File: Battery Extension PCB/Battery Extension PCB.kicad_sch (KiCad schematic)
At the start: 30 parts, among them P1 Solder_Pad, P2 Solder_Pad, U1 M1250RS-02P, U2 S8050, U3 FS8205A, U4 TPS61032PWPR, U5 TP4056, U6 DW01A, U7 FXL0530-6R8-M

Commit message: updated pcb files
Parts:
- H1, H2, H3, H4, H5, H6, H7: footprint footprint:Castellated hole large -> footprint:Castellated hole
- U4: footprint footprint:HTSSOP-16_L5.0-W4.4-P0.65-LS6.4-BL-EP -> Package_SO:HTSSOP-16-1EP_4.4x5mm_P0.65mm_EP3.4x5mm_Mask2.46x2.31mm
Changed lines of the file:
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@@
       (effects (font (size 1.27 1.27)) (justify left))
     )
-    (property "Footprint" "footprint:Castellated hole large" (id 2) (at 207.01 69.85 0)
+    (property "Footprint" "footprint:Castellated hole" (id 2) (at 207.01 69.85 0)
       (effects (font (size 1.27 1.27)) hide)
     )
@@
       (effects (font (size 1.27 1.27)) (justify left))
     )
-    (property "Footprint" "footprint:Castellated hole large" (id 2) (at 207.01 88.9 0)
+    (property "Footprint" "footprint:Castellated hole" (id 2) (at 207.01 88.9 0)
       (effects (font (size 1.27 1.27)) hide)
     )
@@
       (effects (font (size 1.27 1.27)) (justify left))
     )
-    (property "Footprint" "footprint:Castellated hole large" (id 2) (at 207.01 95.25 0)
+    (property "Footprint" "footprint:Castellated hole" (id 2) (at 207.01 95.25 0)
       (effects (font (size 1.27 1.27)) hide)
     )
@@
       (effects (font (size 1.27 1.27)) (justify left))
     )
-    (property "Footprint" "footprint:Castellated hole large" (id 2) (at 207.01 57.15 0)
+    (property "Footprint" "footprint:Castellated hole" (id 2) (at 207.01 57.15 0)
       (effects (font (size 1.27 1.27)) hide)
     )
@@
       (effects (font (size 1.27 1.27)) (justify left))
     )
-    (property "Footprint" "footprint:Castellated hole large" (id 2) (at 207.01 82.55 0)
+    (property "Footprint" "footprint:Castellated hole" (id 2) (at 207.01 82.55 0)
       (effects (font (size 1.27 1.27)) hide)
     )
@@
     (property "Reference" "U4" (id 0) (at 92.71 132.08 0))
     (property "Value" "TPS61032PWPR" (id 1) (at 92.71 134.62 0))
-    (property "Footprint" "footprint:HTSSOP-16_L5.0-W4.4-P0.65-LS6.4-BL-EP" (id 2) (at 92.71 133.35 0)
+    (property "Footprint" "Package_SO:HTSSOP-16-1EP_4.4x5mm_P0.65mm_EP3.4x5mm_Mask2.46x2.31mm" (id 2) (at 92.71 133.35 0)
       (effects (font (size 1.27 1.27) italic) hide)
     )
@@
       (effects (font (size 1.27 1.27)) (justify left))
     )
-    (property "Footprint" "footprint:Castellated hole large" (id 2) (at 207.01 76.2 0)
+    (property "Footprint" "footprint:Castellated hole" (id 2) (at 207.01 76.2 0)
       (effects (font (size 1.27 1.27)) hide)
     )
@@
       (effects (font (size 1.27 1.27)) (justify left))
     )
-    (property "Footprint" "footprint:Castellated hole large" (id 2) (at 207.01 63.5 0)
+    (property "Footprint" "footprint:Castellated hole" (id 2) (at 207.01 63.5 0)
       (effects (font (size 1.27 1.27)) hide)
     )
@@
     )
     (path "/772c5c6f-179b-4fe8-8e39-b42331ec6892"
-      (reference "H1") (unit 1) (value "Castellated_hole") (footprint "footprint:Castellated hole large")
+      (reference "H1") (unit 1) (value "Castellated_hole") (footprint "footprint:Castellated hole")
     )
     (path "/d9dac4f3-7e11-4f08-aac0-c6a976f30cbb"
-      (reference "H2") (unit 1) (value "Castellated_hole") (footprint "footprint:Castellated hole large")
+      (reference "H2") (unit 1) (value "Castellated_hole") (footprint "footprint:Castellated hole")
     )
     (path "/0db3ddba-901d-4b77-a11a-030a5807c4d2"
-      (reference "H3") (unit 1) (value "Castellated_hole") (footprint "footprint:Castellated hole large")
+      (reference "H3") (unit 1) (value "Castellated_hole") (footprint "footprint:Castellated hole")
     )
     (path "/bfa42e2b-26ca-441e-87fc-b5c3c76d771e"
-      (reference "H4") (unit 1) (value "Castellated_hole") (footprint "footprint:Castellated hole large")
+      (reference "H4") (unit 1) (value "Castellated_hole") (footprint "footprint:Castellated hole")
     )
     (path "/a78caffe-a774-45f9-b997-1377730563d7"
-      (reference "H5") (unit 1) (value "Castellated_hole") (footprint "footprint:Castellated hole large")
+      (reference "H5") (unit 1) (value "Castellated_hole") (footprint "footprint:Castellated hole")
     )
     (path "/1972109c-d6a8-439a-8ba3-88c8e6bb7196"
-      (reference "H6") (unit 1) (value "Castellated_hole") (footprint "footprint:Castellated hole large")
+      (reference "H6") (unit 1) (value "Castellated_hole") (footprint "footprint:Castellated hole")
     )
     (path "/37c5e4f3-7cb5-4ef4-9c9d-447ed0599cb8"
-      (reference "H7") (unit 1) (value "Castellated_hole") (footprint "footprint:Castellated hole large")
+      (reference "H7") (unit 1) (value "Castellated_hole") (footprint "footprint:Castellated hole")
     )
     (path "/ae26b445-daff-423c-875c-0c8c4d475a5f"
@@
     )
     (path "/b3294315-f1f5-4699-9d26-423f0a5d1bc5"
-      (reference "U4") (unit 1) (value "TPS61032PWPR") (footprint "footprint:HTSSOP-16_L5.0-W4.4-P0.65-LS6.4-BL-EP")
+      (reference "U4") (unit 1) (value "TPS61032PWPR") (footprint "Package_SO:HTSSOP-16-1EP_4.4x5mm_P0.65mm_EP3.4x5mm_Mask2.46x2.31mm")
     )
     (path "/94c4b137-5d1b-45eb-9fd3-3bc14acb67a1"

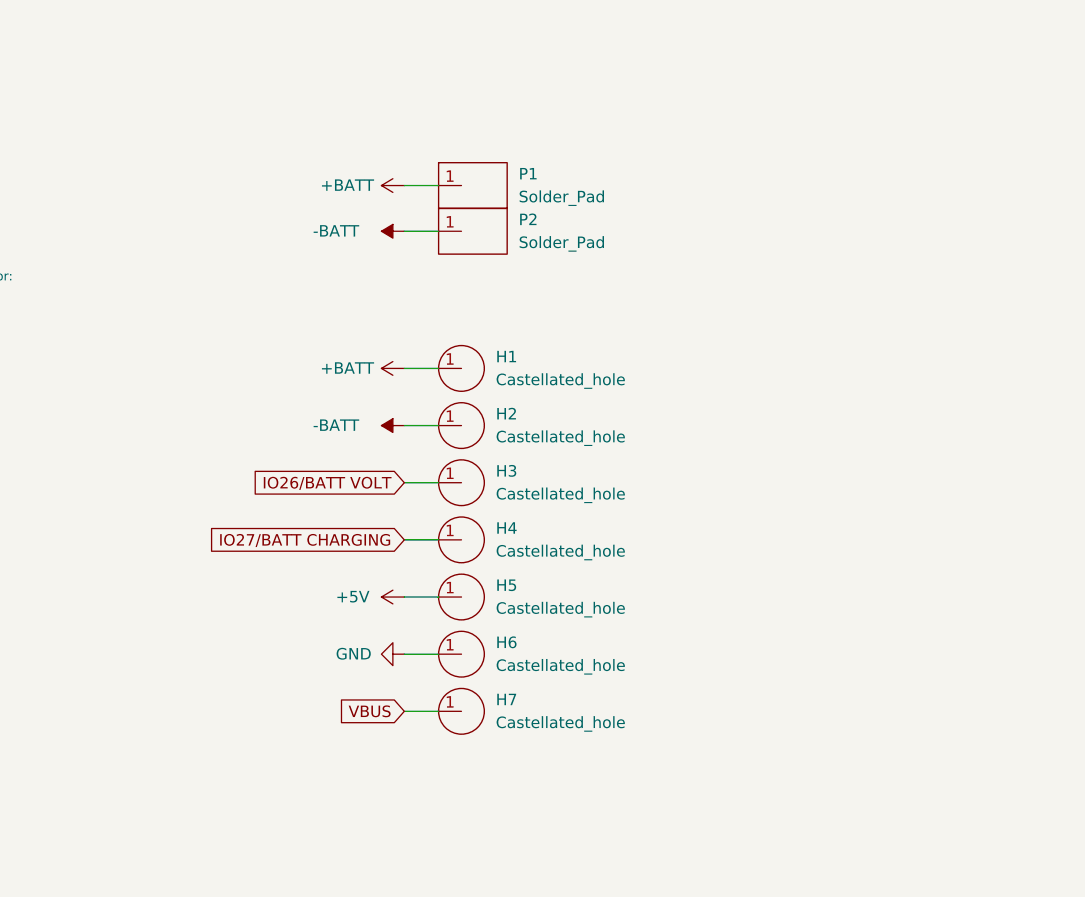
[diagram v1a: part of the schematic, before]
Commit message: replaced castallated holes with solder pads
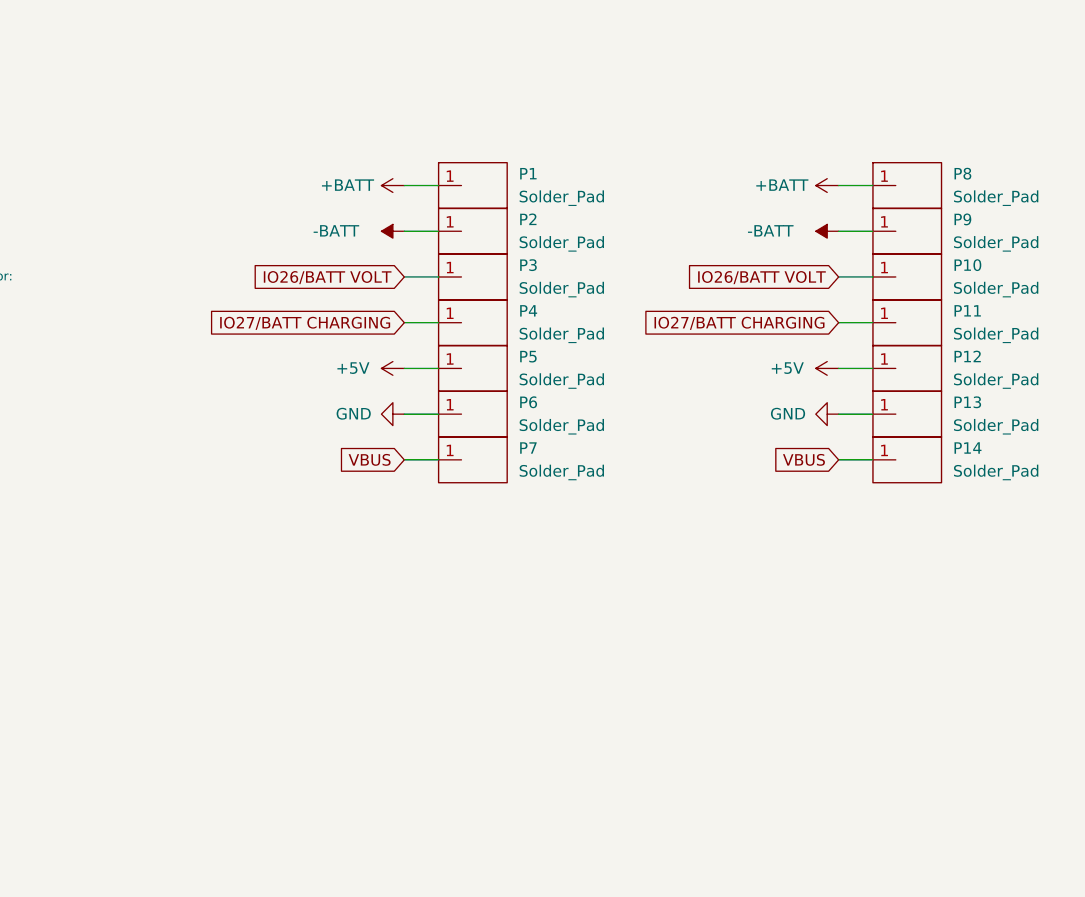
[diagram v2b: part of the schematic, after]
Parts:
- removed H1, H2, H3, H4, H5, H6, H7: Castellated_hole, footprint:Castellated hole, symbol MyParts:Castellated_hole
- added P10, P11, P12, P13, P14, P3, P4, P5, P6, P7, P8, P9: Solder_Pad, footprint:Solder pad, symbol MyParts:Solder_Pad
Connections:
- net +5V: now also P12.1, P5.1
- net +BATT: now also P8.1
- net -BATT: now also P9.1
- net GND: now also P13.1, P6.1
- net IO26/BATT VOLT: now also P10.1, P3.1
- net IO27/BATT CHARGING: now also P11.1, P4.1
- net VBUS: now also P14.1, P7.1

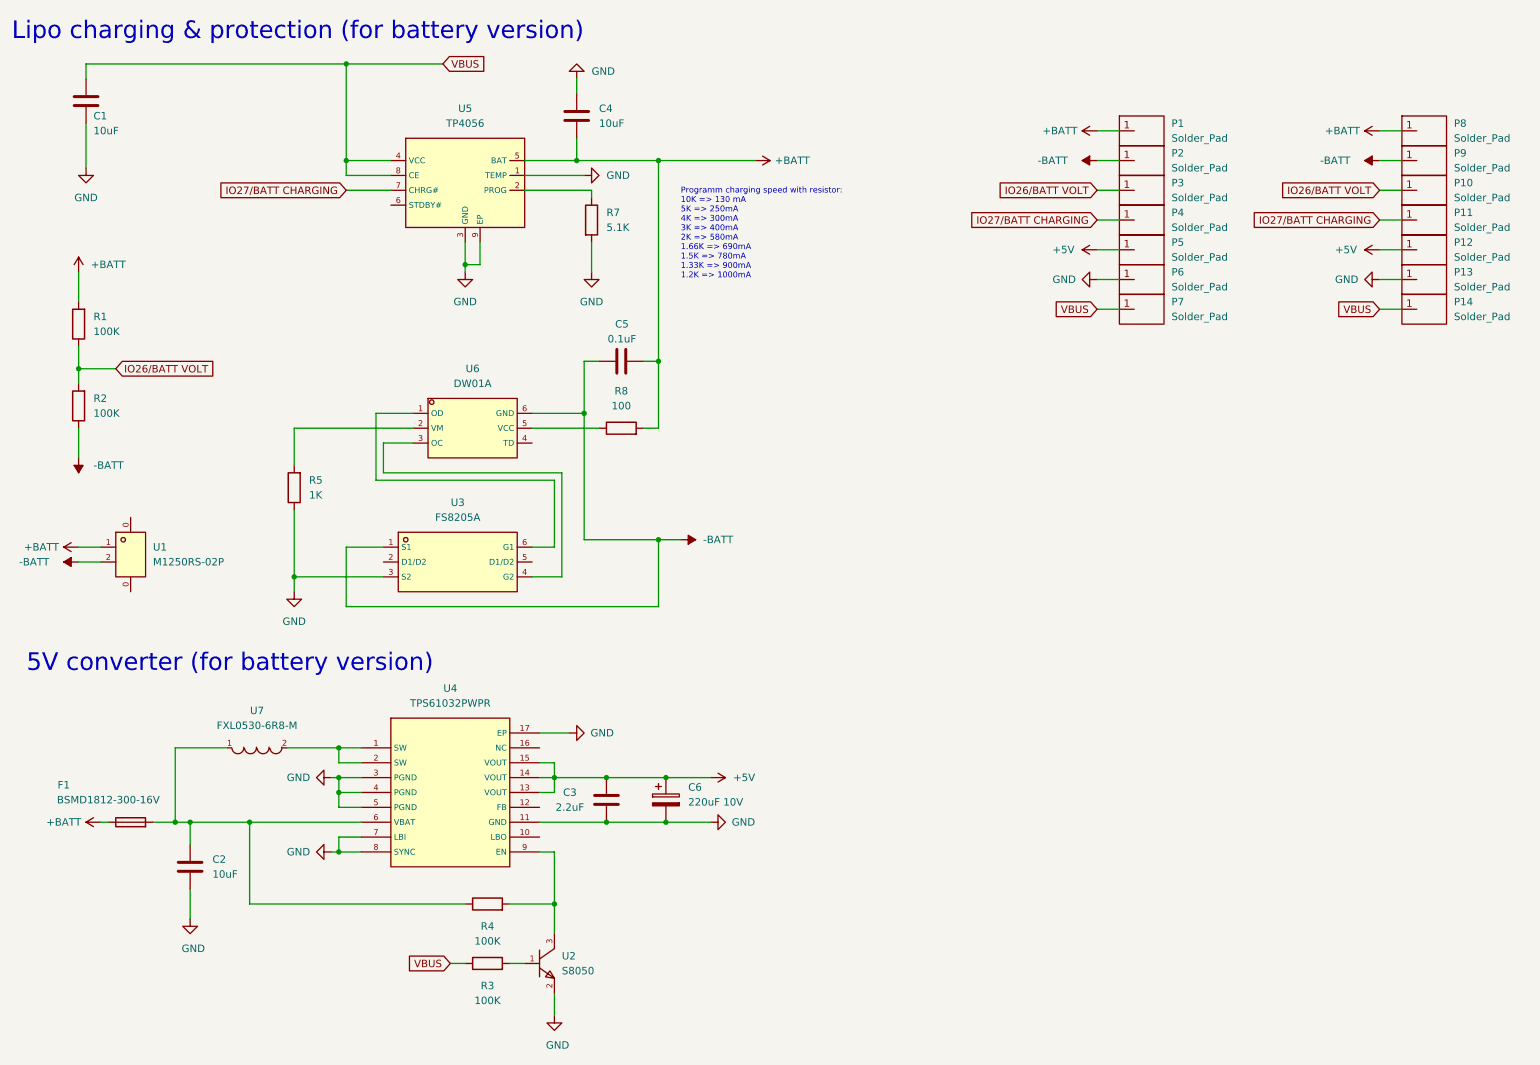
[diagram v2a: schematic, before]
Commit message: fixed battery extension
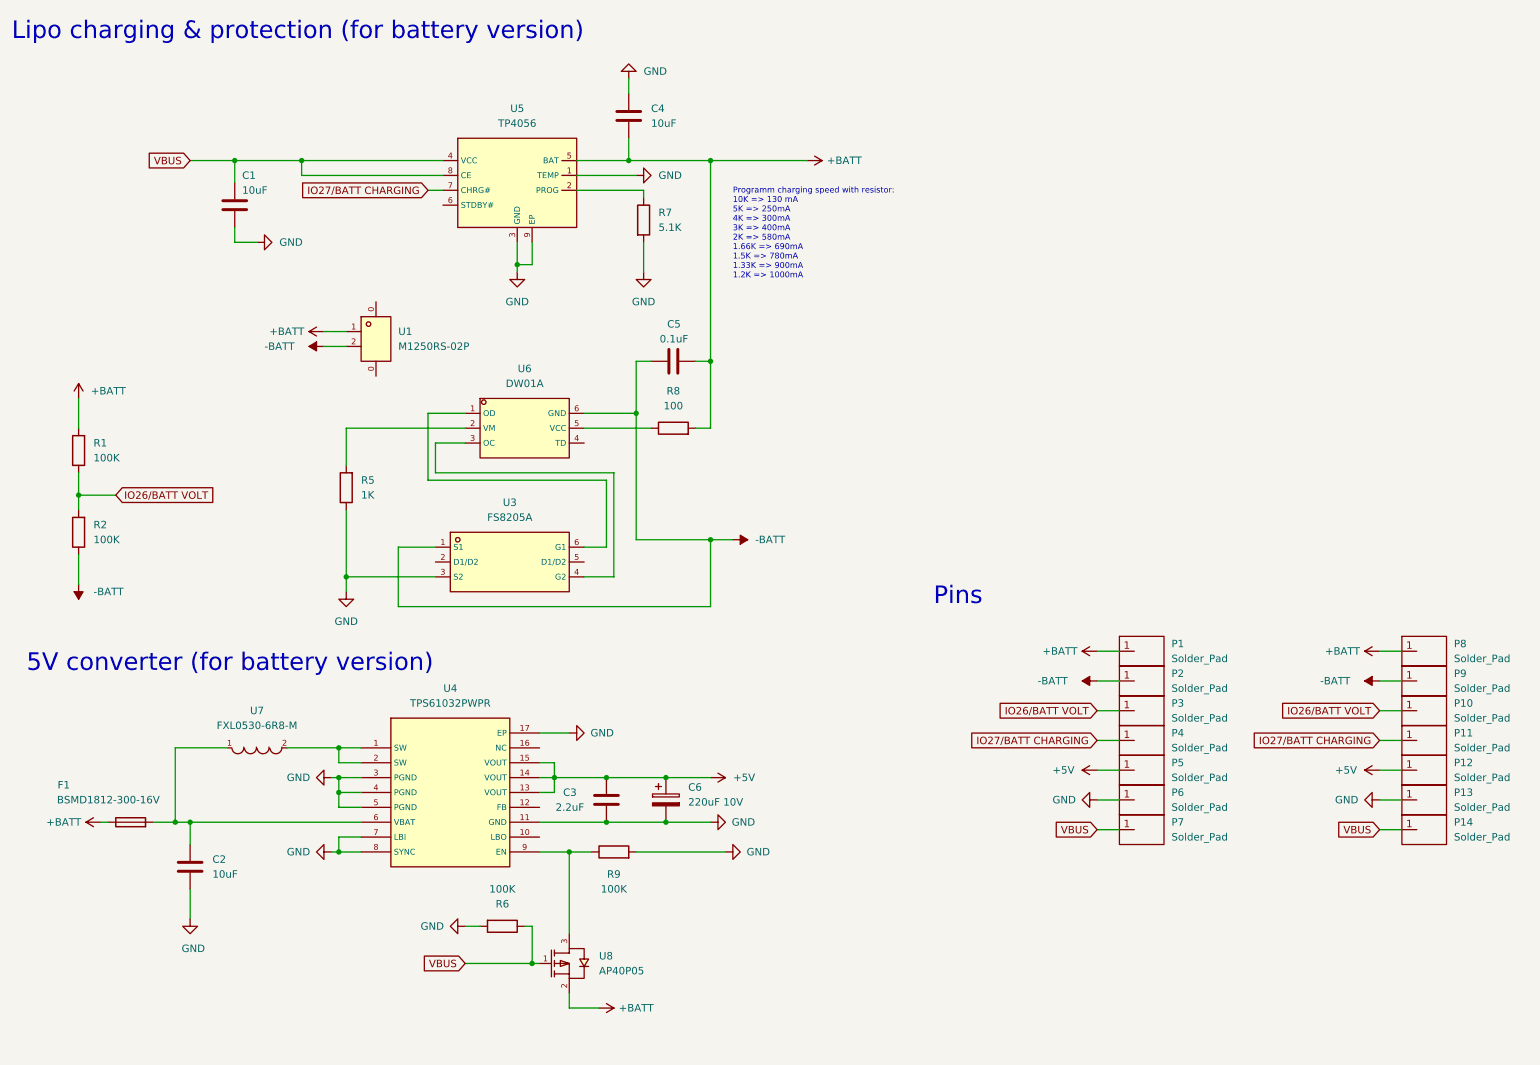
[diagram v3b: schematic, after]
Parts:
- removed R3, R4: 100K, Resistor_SMD:R_0603_1608Metric_Pad0.98x0.95mm_HandSolder, symbol Device:R
- removed U2: S8050, footprint:SOT-23-3_L3.0-W1.7-P0.95-LS2.9-BR, symbol MyParts:S8050
- added R6, R9: 100K, Resistor_SMD:R_0603_1608Metric_Pad0.98x0.95mm_HandSolder, symbol Device:R
- added U8: AP40P05, footprint:SOT-23-3_L2.9-W1.3-P1.90-LS2.4-BR, symbol MyParts:AP40P05
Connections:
- net +BATT: now also U8.2 (S)
- net GND: now also R6.2, R9.2
- net VBUS: now also R6.1, U8.1 (G)
- net at U4.9 (EN): now also R9.1, U8.3 (D)
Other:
- note added: "Pins"
- moved on the sheet: C1, C4, C5, P1, P10, P11, P12, P13, P14, P2, P3, P4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

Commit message: replaced 0603 with 0402 (battery extension)
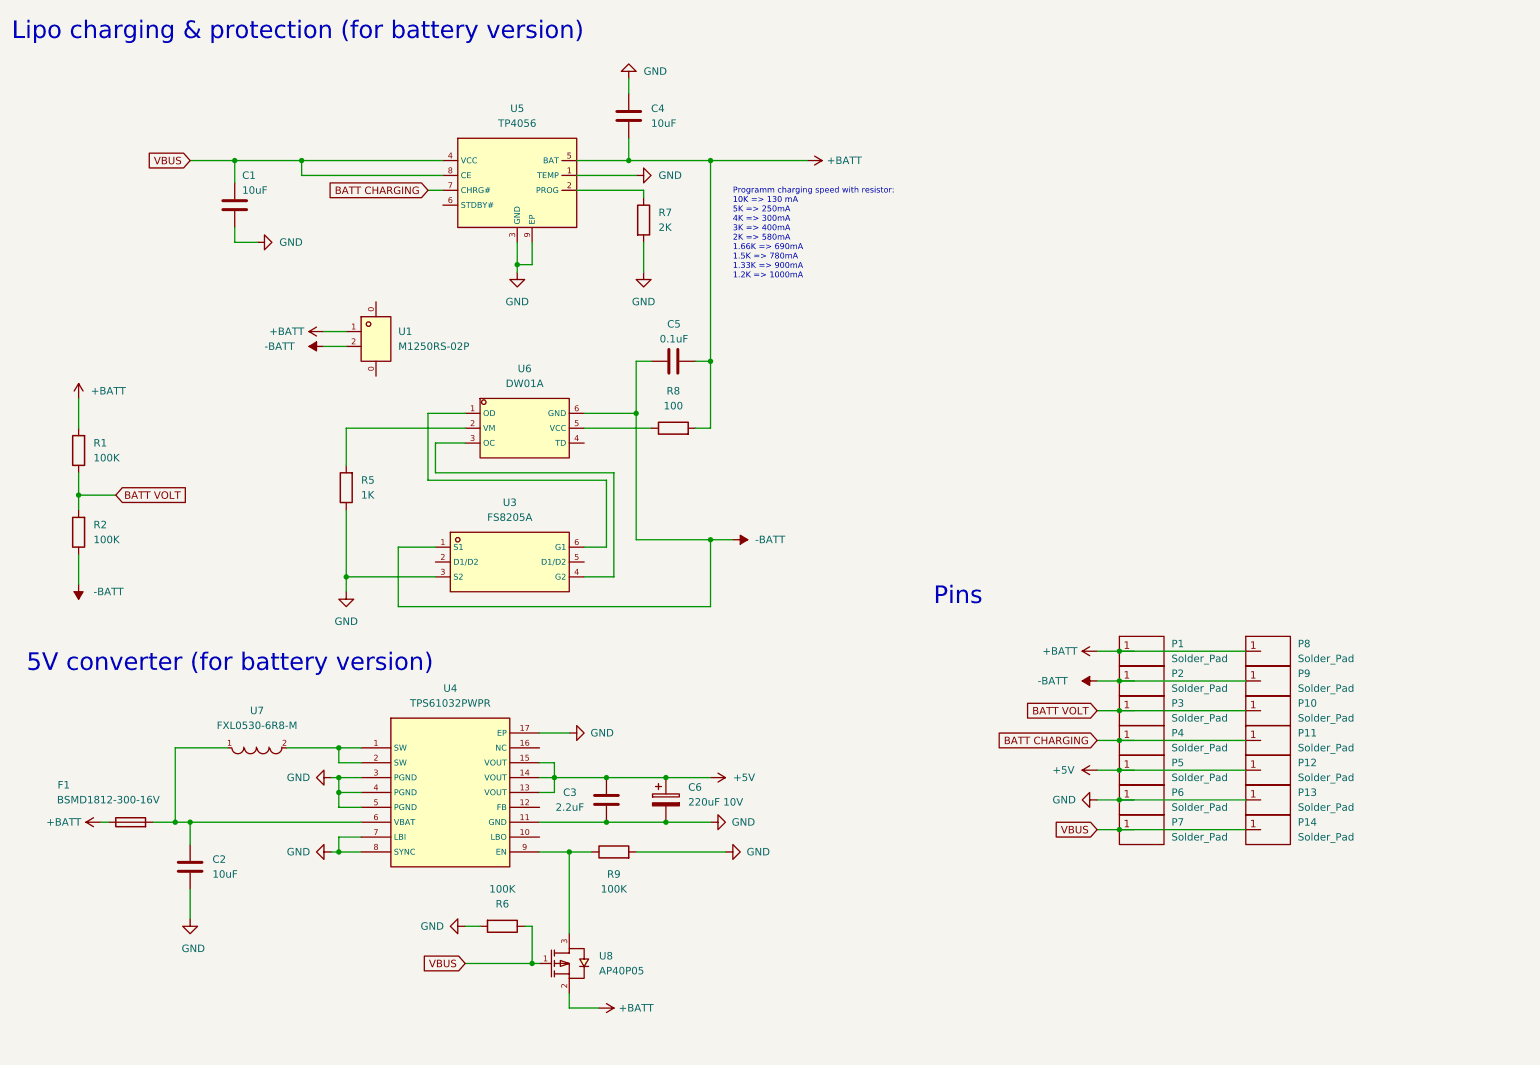
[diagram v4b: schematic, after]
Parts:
- C1, C2, C4: footprint Capacitor_SMD:C_0603_1608Metric_Pad1.08x0.95mm_HandSolder -> Capacitor_SMD:C_0603_1608Metric; LCSC # C19702 -> C96446
- C3: footprint Capacitor_SMD:C_0603_1608Metric_Pad1.08x0.95mm_HandSolder -> Capacitor_SMD:C_0603_1608Metric
- C5: footprint Capacitor_SMD:C_0603_1608Metric_Pad1.08x0.95mm_HandSolder -> Capacitor_SMD:C_0402_1005Metric; LCSC # C14663 -> C1525
- C6: LCSC # (none) -> C267466; LCSC Part # C267466 -> (none)
- R1, R2, R6, R9: footprint Resistor_SMD:R_0603_1608Metric_Pad0.98x0.95mm_HandSolder -> Resistor_SMD:R_0402_1005Metric; LCSC # C25803 -> C25741
- R5: footprint Resistor_SMD:R_0603_1608Metric_Pad0.98x0.95mm_HandSolder -> Resistor_SMD:R_0402_1005Metric; LCSC # C21190 -> C11702
- R7: value 5.1K -> 2K; footprint Resistor_SMD:R_0603_1608Metric_Pad0.98x0.95mm_HandSolder -> Resistor_SMD:R_0402_1005Metric; LCSC # C23186 -> C4109
- R8: footprint Resistor_SMD:R_0603_1608Metric_Pad0.98x0.95mm_HandSolder -> Resistor_SMD:R_0402_1005Metric; LCSC # C22775 -> C25076
- U4: LCSC C88716 -> (none); LCSC # (none) -> C88716
- U7: LCSC C177249 -> (none); LCSC # (none) -> C177249
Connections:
- net IO26/BATT VOLT renamed BATT VOLT
- net IO27/BATT CHARGING renamed BATT CHARGING
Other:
- moved on the sheet: P10, P11, P12, P13, P14, P8, P9
